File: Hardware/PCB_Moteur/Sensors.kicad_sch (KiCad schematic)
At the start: 19 parts, among them U7 INA125UA/2K5, U8 INA125UA/2K5, U9 MAX6612MXK

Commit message: wip : add final footprint to lib and start pcb
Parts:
- gave numbers to parts that had none: 2
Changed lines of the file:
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@@
 		(on_board yes)
 		(dnp no)
-		(property "Reference" "J?"
+		(property "Reference" "J18"
 			(at 128.27 111.252 0)
 			(effects
@@
 			(project "PCB_moteur"
 				(path "/b0d87684-7b1c-41d8-8358-755aa327573e/f31687d3-ca84-4d71-914a-32b6c2b363a9"
-					(reference "J?")
+					(reference "J18")
 					(unit 1)
 				)
@@
 		(on_board yes)
 		(dnp no)
-		(property "Reference" "J?"
+		(property "Reference" "J19"
 			(at 128.778 35.814 0)
 			(effects
@@
 			(project "PCB_moteur"
 				(path "/b0d87684-7b1c-41d8-8358-755aa327573e/f31687d3-ca84-4d71-914a-32b6c2b363a9"
-					(reference "J?")
-					(unit 1)
-				)
+					(reference "J19")
+					(unit 1)
+				)

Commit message: tout les footprint son prêt
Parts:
- U7, U8: footprint pcb_moteur:INA125UA_2K5-M -> pcb_moteur:D16-L; DigiKey_Part_Number  (none) -> 296-50343-1-ND; Doc (none) -> https://www.ti.com/lit/gpn/ina125; Manufacturer_Part_Number (none) -> INA125UA/2K5
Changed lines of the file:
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@@
 	)
 	(symbol
+		(lib_name "INA125UA_2K5_1")
 		(lib_id "pcb_moteur:INA125UA_2K5")
 		(at 43.18 50.8 0)
@@
 			)
 		)
-		(property "Footprint" "pcb_moteur:INA125UA_2K5-M"
-			(at 43.18 50.8 0)
-			(effects
-				(font
-					(size 1.27 1.27)
-					(italic yes)
-				)
-				(hide yes)
-			)
-		)
-		(property "Datasheet" "https://www.ti.com/lit/gpn/ina125"
-			(at 43.18 50.8 0)
-			(effects
-				(font
-					(size 1.27 1.27)
-					(italic yes)
-				)
-				(hide yes)
-			)
-		)
-		(property "Description" ""
+		(property "Footprint" "pcb_moteur:D16-L"
+			(at 43.18 50.8 0)
+			(effects
+				(font
+					(size 1.27 1.27)
+				)
+				(hide yes)
+			)
+		)
+		(property "Datasheet" "https://www.digikey.ca/en/products/detail/texas-instruments/INA125UA-2K5/300987"
+			(at 43.18 50.8 0)
+			(effects
+				(font
+					(size 1.27 1.27)
+				)
+				(hide yes)
+			)
+		)
+		(property "Description" "IC INST AMP 1 CIRCUIT 16SOIC"
+			(at 43.18 50.8 0)
+			(effects
+				(font
+					(size 1.27 1.27)
+				)
+				(hide yes)
+			)
+		)
+		(property "Doc" "https://www.ti.com/lit/gpn/ina125"
+			(at 43.18 50.8 0)
+			(effects
+				(font
+					(size 1.27 1.27)
+				)
+				(hide yes)
+			)
+		)
+		(property "DigiKey_Part_Number " "296-50343-1-ND"
+			(at 43.18 50.8 0)
+			(effects
+				(font
+					(size 1.27 1.27)
+				)
+				(hide yes)
+			)
+		)
+		(property "Manufacturer_Part_Number" "INA125UA/2K5"
 			(at 43.18 50.8 0)
 			(effects
@@
 			)
 		)
-		(property "Footprint" "pcb_moteur:INA125UA_2K5-M"
-			(at 41.91 125.73 0)
-			(effects
-				(font
-					(size 1.27 1.27)
-					(italic yes)
-				)
-				(hide yes)
-			)
-		)
-		(property "Datasheet" "https://www.ti.com/lit/gpn/ina125"
-			(at 41.91 125.73 0)
-			(effects
-				(font
-					(size 1.27 1.27)
-					(italic yes)
-				)
-				(hide yes)
-			)
-		)
-		(property "Description" ""
-			(at 41.91 125.73 0)
-			(effects
+		(property "Footprint" "pcb_moteur:D16-L"
+			(at 41.91 125.73 0)
+			(effects
+				(font
+					(size 1.27 1.27)
+				)
+				(hide yes)
+			)
+		)
+		(property "Datasheet" "https://www.digikey.ca/en/products/detail/texas-instruments/INA125UA-2K5/300987"
+			(at 41.91 125.73 0)
+			(effects
+				(font
+					(size 1.27 1.27)
+				)
+				(hide yes)
+			)
+		)
+		(property "Description" "IC INST AMP 1 CIRCUIT 16SOIC"
+			(at 41.91 125.73 0)
+			(effects
+				(font
+					(size 1.27 1.27)
+				)
+				(hide yes)
+			)
+		)
+		(property "Doc" "https://www.ti.com/lit/gpn/ina125"
+			(at 41.91 125.73 0)
+			(effects
+				(font
+					(size 1.27 1.27)
+				)
+				(hide yes)
+			)
+		)
+		(property "DigiKey_Part_Number " "296-50343-1-ND"
+			(at 41.91 125.73 0)
+			(effects
+				(font
+					(size 1.27 1.27)
+				)
+				(hide yes)
+			)
+		)
+		(property "Manufacturer_Part_Number" "INA125UA/2K5"
+			(at 41.91 125.73 0)
+			(effects

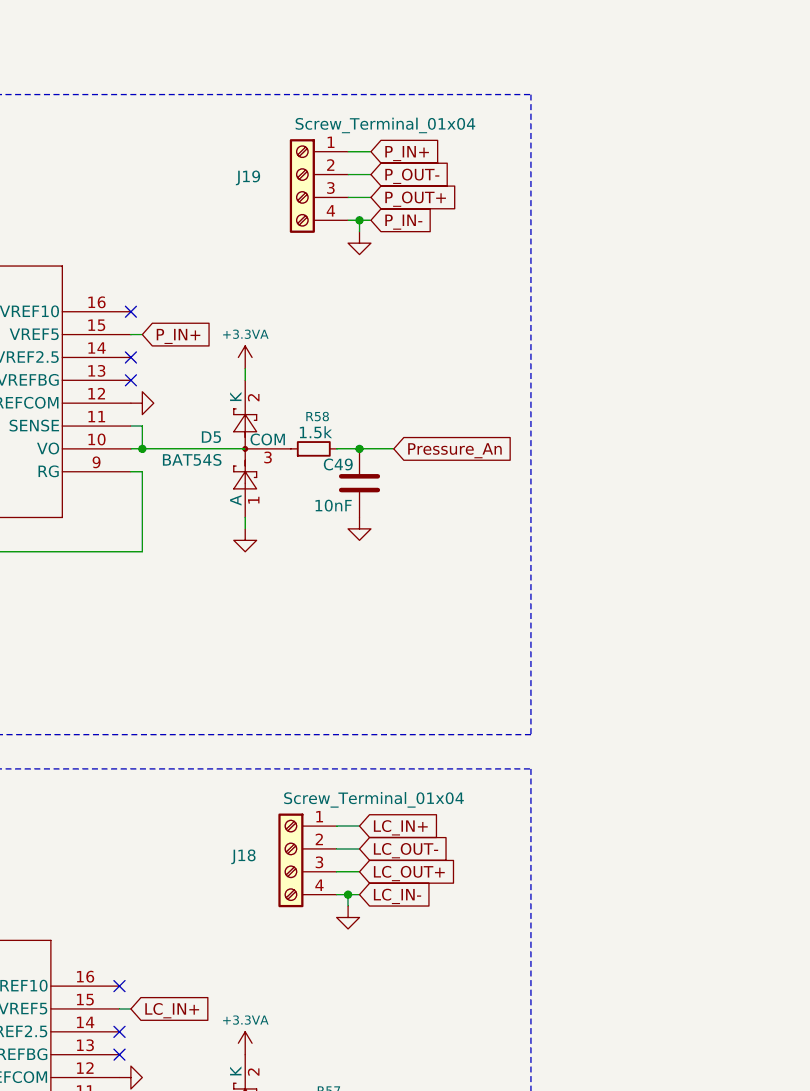
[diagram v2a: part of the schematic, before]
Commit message: Layout Alim 3.3V + pression et loadcell
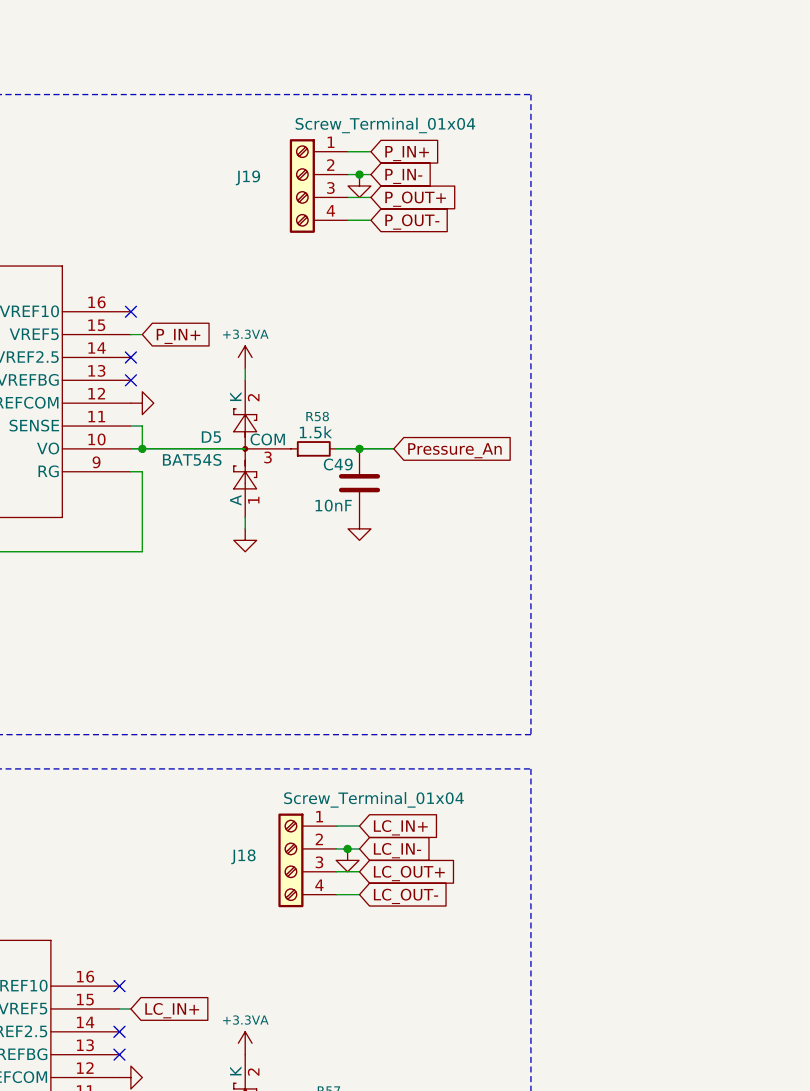
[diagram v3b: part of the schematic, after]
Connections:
- net GND: now also J18.2 (Pin_2), J19.2 (Pin_2); no longer J18.4 (Pin_4), J19.4 (Pin_4)
- net LC_OUT-: now also J18.4 (Pin_4); no longer J18.2 (Pin_2)
- net P_OUT-: now also J19.4 (Pin_4); no longer J19.2 (Pin_2)

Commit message: wip: layout circuits Pyro
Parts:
- R57, R58: footprint Resistor_SMD:R_0603_1608Metric -> Resistor_SMD:R_0805_2012Metric
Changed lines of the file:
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@@
 			)
 		)
-		(property "Footprint" "Resistor_SMD:R_0603_1608Metric"
+		(property "Footprint" "Resistor_SMD:R_0805_2012Metric"
 			(at 135.89 140.97 0)
 			(effects
@@
 			)
 		)
-		(property "Footprint" "Resistor_SMD:R_0603_1608Metric"
+		(property "Footprint" "Resistor_SMD:R_0805_2012Metric"
 			(at 134.62 66.04 0)
 			(effects

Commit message: wip: layout presque fini (decoup stm32 restant)
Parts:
- C46, C48: footprint Capacitor_SMD:C_0805_2012Metric -> Capacitor_SMD:C_0603_1608Metric
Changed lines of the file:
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@@
 			)
 		)
-		(property "Footprint" "Capacitor_SMD:C_0805_2012Metric"
+		(property "Footprint" "Capacitor_SMD:C_0603_1608Metric"
 			(at 258.7752 48.26 0)
 			(effects
@@
 			)
 		)
-		(property "Footprint" "Capacitor_SMD:C_0805_2012Metric"
+		(property "Footprint" "Capacitor_SMD:C_0603_1608Metric"
 			(at 143.2052 148.59 0)
 			(effects

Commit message: wip: début routing
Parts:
- C48: value 10nF -> 100nF; footprint Capacitor_SMD:C_0603_1608Metric -> Capacitor_SMD:C_0805_2012Metric
- C49: value 10nF -> 100nF
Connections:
- net at D5.3 (COM), R58.1: now also U7.10 (VO), U7.11 (SENSE)
- net at D6.3 (COM), R57.1: now also U8.10 (VO), U8.11 (SENSE)
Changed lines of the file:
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@@
+	)
+	(junction
+		(at 142.24 140.97)
+		(diameter 0)
+		(color 0 0 0 0)
+	)
+	(junction
+		(at 220.98 49.53)
+		(diameter 0)
+		(color 0 0 0 0)
+	)
+	(junction
+		(at 34.29 128.27)
+		(diameter 0)
+		(color 0 0 0 0)
+	)
+	(junction
+		(at 132.08 66.04)
+		(diameter 0)
+		(color 0 0 0 0)
+	)
+	(junction
+		(at 139.7 66.04)
+		(diameter 0)
+		(color 0 0 0 0)
 	)
 	(junction
@@
 	)
 	(junction
-		(at 142.24 140.97)
+		(at 43.18 44.45)
 		(diameter 0)
 		(color 0 0 0 0)
 	)
 	(junction
-		(at 220.98 49.53)
-		(diameter 0)
-		(color 0 0 0 0)
-	)
-	(junction
-		(at 34.29 128.27)
-		(diameter 0)
-		(color 0 0 0 0)
-	)
-	(junction
-		(at 139.7 66.04)
-		(diameter 0)
-		(color 0 0 0 0)
-	)
-	(junction
-		(at 43.18 44.45)
+		(at 132.08 140.97)
 		(diameter 0)
 		(color 0 0 0 0)
@@
 	(wire
 		(pts
-			(xy 114.3 140.97) (xy 113.03 140.97)
-		)
-		(stroke
-			(width 0)
-			(type default)
-		)
-	)
-	(wire
-		(pts
 			(xy 257.81 39.37) (xy 269.24 39.37)
 		)
@@
 	(wire
 		(pts
-			(xy 114.3 140.97) (xy 127 140.97)
+			(xy 113.03 140.97) (xy 114.3 140.97)
 		)
 		(stroke
@@
 	(wire
 		(pts
+			(xy 114.3 140.97) (xy 132.08 140.97)
+		)
+		(stroke
+			(width 0)
+			(type default)
+		)
+	)
+	(wire
+		(pts
 			(xy 267.97 34.29) (xy 266.7 34.29)
 		)
@@
 	(wire
 		(pts
-			(xy 133.35 140.97) (xy 132.08 140.97)
-		)
-		(stroke
-			(width 0)
-			(type default)
-		)
-	)
-	(wire
-		(pts
 			(xy 43.18 50.8) (xy 43.18 44.45)
 		)
@@
 	(wire
 		(pts
+			(xy 132.08 140.97) (xy 133.35 140.97)
+		)
+		(stroke
+			(width 0)
+			(type default)
+		)
+	)
+	(wire
+		(pts
 			(xy 83.82 77.47) (xy 115.57 77.47)
 		)
@@
 	(wire
 		(pts
-			(xy 115.57 66.04) (xy 127 66.04)
+			(xy 115.57 66.04) (xy 132.08 66.04)
 		)
 		(stroke
@@
 			)
 		)
-		(property "Value" "10nF"
+		(property "Value" "100nF"
 			(at 134.62 72.39 0)
 			(effects
@@
 			)
 		)
-		(property "Value" "10nF"
+		(property "Value" "100nF"
 			(at 137.16 147.066 0)
 			(effects
@@
 			)
 		)
-		(property "Footprint" "Capacitor_SMD:C_0603_1608Metric"
+		(property "Footprint" "Capacitor_SMD:C_0805_2012Metric"
 			(at 143.2052 148.59 0)
 			(effects

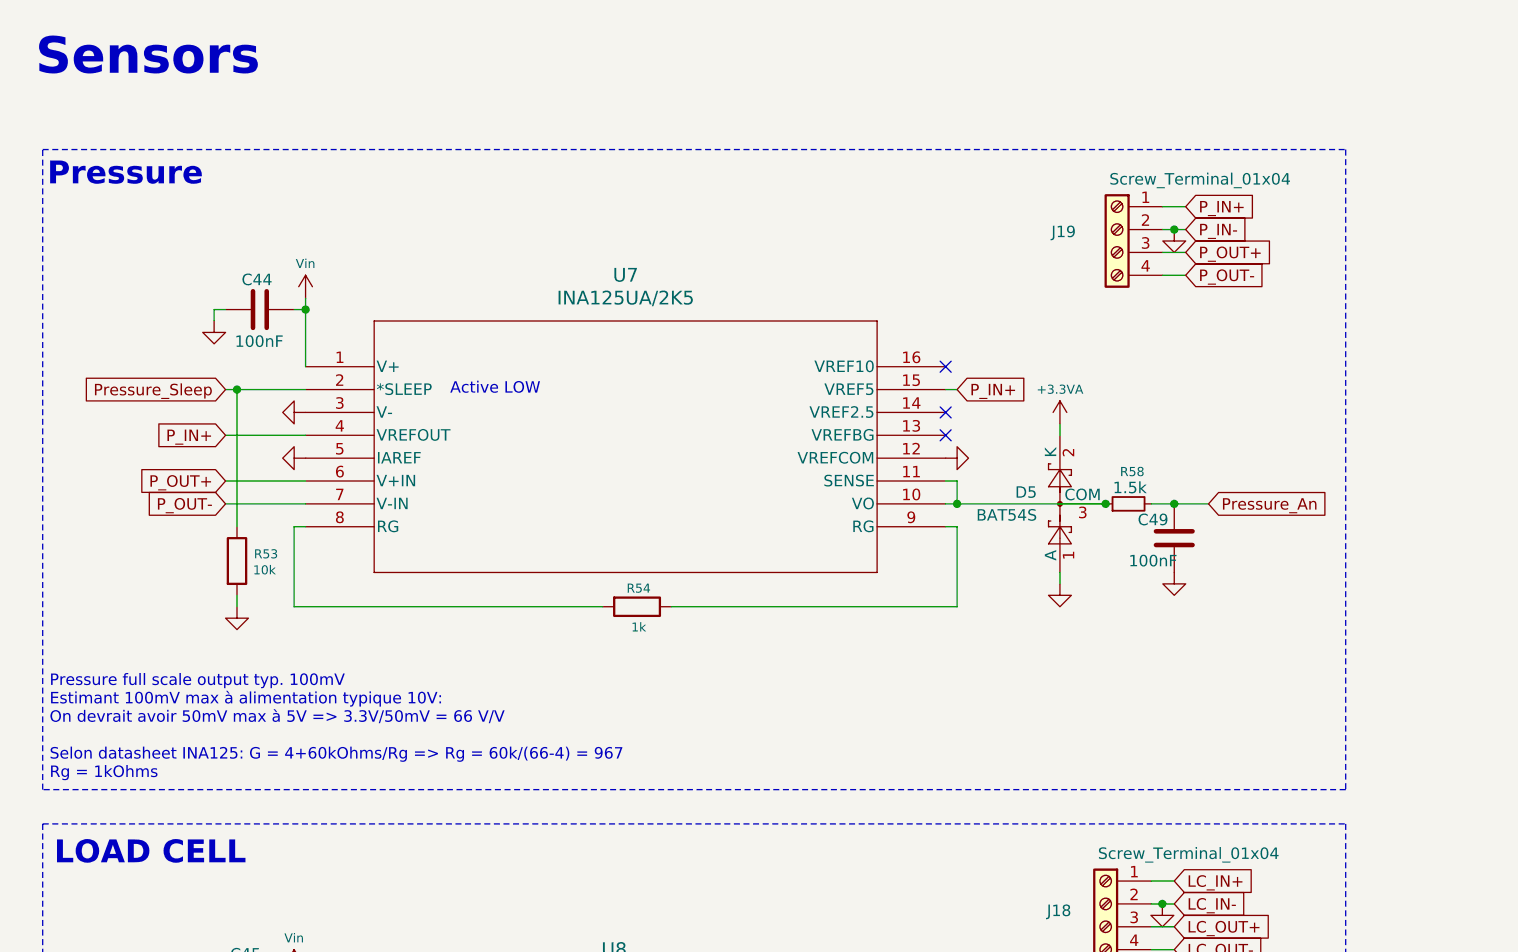
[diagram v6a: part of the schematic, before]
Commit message: wip: separation GND et modif schéma pression
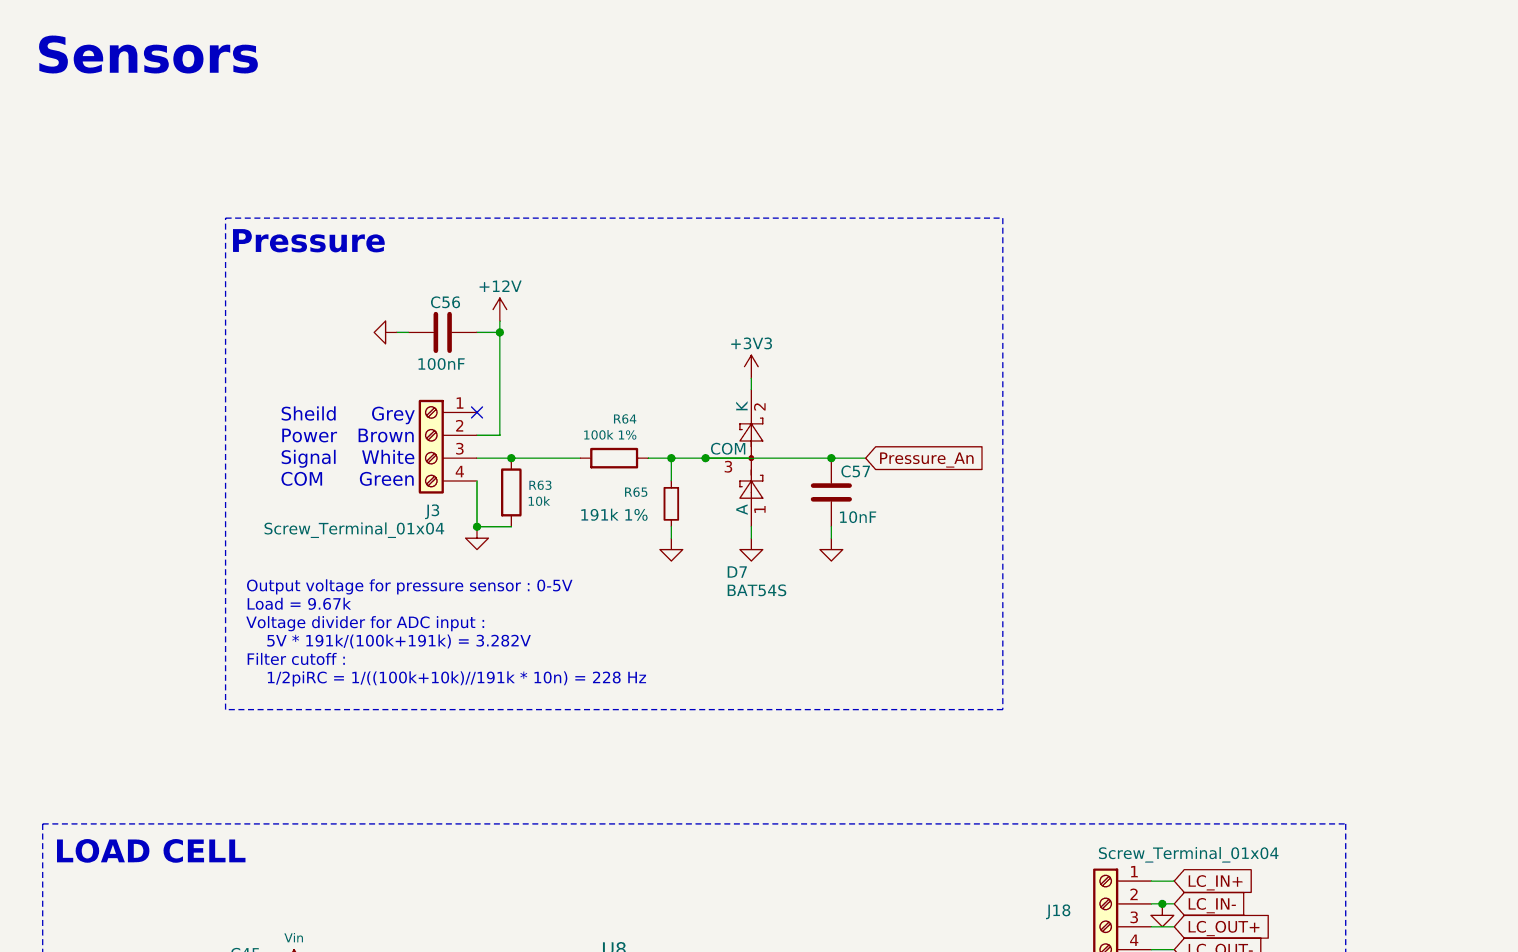
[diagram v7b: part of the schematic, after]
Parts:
- removed C44, C49: 100nF, Capacitor_SMD:C_0805_2012Metric, symbol Device:C
- removed D5: BAT54S, Package_TO_SOT_SMD:SOT-23, symbol Diode:BAT54S
- removed J19: Screw_Terminal_01x04, pcb_moteur:CONN_OSTVN04A150_OST, symbol Connector:Screw_Terminal_01x04
- removed R53: 10k, Resistor_SMD:R_0805_2012Metric, symbol Device:R
- removed R54: 1k, Resistor_SMD:R_0805_2012Metric, symbol Device:R
- removed R58: 1.5k, Resistor_SMD:R_0805_2012Metric, symbol Device:R_Small
- removed U7: INA125UA/2K5, pcb_moteur:D16-L, symbol pcb_moteur:INA125UA_2K5
- added C56: 100nF, Capacitor_SMD:C_0603_1608Metric, symbol Device:C
- added C57: 10nF, Capacitor_SMD:C_0805_2012Metric, symbol Device:C
- added D7: BAT54S, Package_TO_SOT_SMD:SOT-23, symbol Diode:BAT54S
- added J3: Screw_Terminal_01x04, pcb_moteur:CONN_OSTVN04A150_OST, symbol Connector:Screw_Terminal_01x04
- added R63: 10k, Resistor_SMD:R_0805_2012Metric, symbol Device:R
- added R64: 100k 1%, Resistor_SMD:R_0805_2012Metric, symbol Device:R
- added R65: 191k 1%, Resistor_SMD:R_0805_2012Metric, symbol Device:R_Small
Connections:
- net +3V3: now also D7.2 (K)
- net GND: now also C56.1, C57.2, D7.1 (A), J3.4 (Pin_4), R63.2, R65.2
- net Pressure_An: now also C57.1, D7.3 (COM), R64.1, R65.1
- new net: J3.3 (Pin_3), R63.1, R64.2
- new net +12V: C56.2, J3.2 (Pin_2)
- no-connect marks 6 -> 4
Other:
- note added: "Grey Brown White Green"
- note added: "Output voltage for pressure sensor : 0-5V Load = 9.67k Voltage divider for ADC input : 5V * 191k/(100k+191k) = 3.282V Filter cutoff : 1/2piRC = 1/((100k+10k)//191k * 10n) = 228 Hz"
- note added: "Sheild Power Signal COM"
- note removed: "Pressure full scale output typ. 100mV Estimant 100mV max à alimentation typique 10V: On devrait avoir 50mV max à 5V => 3.3V/50mV = 66 V/V Selon datasheet INA125: G = 4+60kOhms/Rg => Rg = 60k/(66-4) = 967 Rg = 1kOhms"

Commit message: wip: new pressure et fix alim
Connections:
- net +12V is gone; now on net Vin: C56.2, J3.2 (Pin_2)
- net +3.3VA is gone; now on net +3V3: D6.2 (K)
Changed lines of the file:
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@@
 	)
 	(symbol
-		(lib_id "power:+3.3VA")
+		(lib_id "power:+3V3")
 		(at 127 133.35 0)
-		(unit 1)
-		(exclude_from_sim no)
-		(in_bom yes)
-		(on_board yes)
-		(dnp no)
-		(property "Reference" "#PWR075"
+		(mirror y)
+		(unit 1)
+		(exclude_from_sim no)
+		(in_bom yes)
+		(on_board yes)
+		(dnp no)
+		(property "Reference" "#PWR037"
 			(at 127 137.16 0)
 			(effects
 				(font
-					(size 1 1)
-				)
-				(hide yes)
-			)
-		)
-		(property "Value" "+3.3VA"
+					(size 1.27 1.27)
+				)
+				(hide yes)
+			)
+		)
+		(property "Value" "+3V3"
 			(at 127 129.54 0)
 			(effects
 				(font
-					(size 1 1)
+					(size 1.27 1.27)
 				)
 			)
@@
 			(effects
 				(font
-					(size 1 1)
+					(size 1.27 1.27)
 				)
 				(hide yes)
@@
 			(effects
 				(font
-					(size 1 1)
-				)
-				(hide yes)
-			)
-		)
-		(property "Description" ""
+					(size 1.27 1.27)
+				)
+				(hide yes)
+			)
+		)
+		(property "Description" "Power symbol creates a global label with name \"+3V3\""
 			(at 127 133.35 0)
 			(effects
@@
 					(size 1.27 1.27)
 				)
-			)
-		)
-		(pin "1"
-		)
-		(instances
-			(project "PCB_moteur"
-				(path "/b0d87684-7b1c-41d8-8358-755aa327573e/f31687d3-ca84-4d71-914a-32b6c2b363a9"
-					(reference "#PWR075")
+				(hide yes)
+			)
+		)
+		(pin "1"
+		)
+		(instances
+			(project "PCB_moteur"
+				(path "/b0d87684-7b1c-41d8-8358-755aa327573e/f31687d3-ca84-4d71-914a-32b6c2b363a9"
+					(reference "#PWR037")
 					(unit 1)
 				)
@@
 	)
 	(symbol
-		(lib_name "+12V_1")
-		(lib_id "power:+12V")
-		(at 64.77 45.72 0)
-		(unit 1)
-		(exclude_from_sim no)
-		(in_bom yes)
-		(on_board yes)
-		(dnp no)
-		(property "Reference" "#PWR0146"
-			(at 64.77 49.53 0)
-			(effects
-				(font
-					(size 1.27 1.27)
-				)
-				(hide yes)
-			)
-		)
-		(property "Value" "+12V"
-			(at 64.77 41.91 0)
-			(effects
-				(font
-					(size 1.27 1.27)
-				)
-			)
-		)
-		(property "Footprint" ""
-			(at 64.77 45.72 0)
-			(effects
-				(font
-					(size 1.27 1.27)
-				)
-				(hide yes)
-			)
-		)
-		(property "Datasheet" ""
-			(at 64.77 45.72 0)
-			(effects
-				(font
-					(size 1.27 1.27)
-				)
-				(hide yes)
-			)
-		)
-		(property "Description" "Power symbol creates a global label with name \"+12V\""
-			(at 64.77 45.72 0)
-			(effects
-				(font
-					(size 1.27 1.27)
-				)
-				(hide yes)
-			)
-		)
-		(pin "1"
-		)
-		(instances
-			(project "PCB_moteur"
-				(path "/b0d87684-7b1c-41d8-8358-755aa327573e/f31687d3-ca84-4d71-914a-32b6c2b363a9"
-					(reference "#PWR0146")
-					(unit 1)
-				)
-			)
-		)
-	)
-	(symbol
 		(lib_id "power:GND")
 		(at 101.6 69.85 0)
@@
 					(unit 1)
 				)
+			)
+		)
+	)
+	(symbol
+		(lib_id "power:+12V")
+		(at 64.77 45.72 0)
+		(unit 1)
+		(exclude_from_sim no)
+		(in_bom yes)
+		(on_board yes)
+		(dnp no)
+		(property "Reference" "#PWR07"
+			(at 64.77 49.53 0)
+			(effects
+				(font
+					(size 1 1)
+				)
+				(hide yes)
+			)
+		)
+		(property "Value" "Vin"
+			(at 64.77 41.91 0)
+			(effects
+				(font
+					(size 1 1)
+				)
+			)
+		)
+		(property "Footprint" ""
+			(at 64.77 45.72 0)
+			(effects
+				(font
+					(size 1 1)
+				)
+				(hide yes)
+			)
+		)
+		(property "Datasheet" ""
+			(at 64.77 45.72 0)
+			(effects
+				(font
+					(size 1 1)
+				)
+				(hide yes)
+			)
+		)
+		(property "Description" ""
+			(at 64.77 45.72 0)
+			(effects
+				(font
+					(size 1.27 1.27)
+				)
+				(hide yes)
+			)
+		)
+		(pin "1"
+		)
+		(instances
+			(project "PCB_moteur"
+				(path "/b0d87684-7b1c-41d8-8358-755aa327573e/f31687d3-ca84-4d71-914a-32b6c2b363a9"
+					(reference "#PWR07")
+					(unit 1)
+				)
